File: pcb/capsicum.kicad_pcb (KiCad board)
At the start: 2 copper layers, 68.6 x 88.9 mm, 70 parts, among them J2 Screw terminal, J3 USB-C 16+8 USB 2.0, Q1 NS2101P, Q2 BC817, SW1 SW_SPDT, SW3 SW_SPDT, U1 ESP32-C3-WROOM-02, U2 TQ33E-1, U3 AP2112K, U4 MCP73831

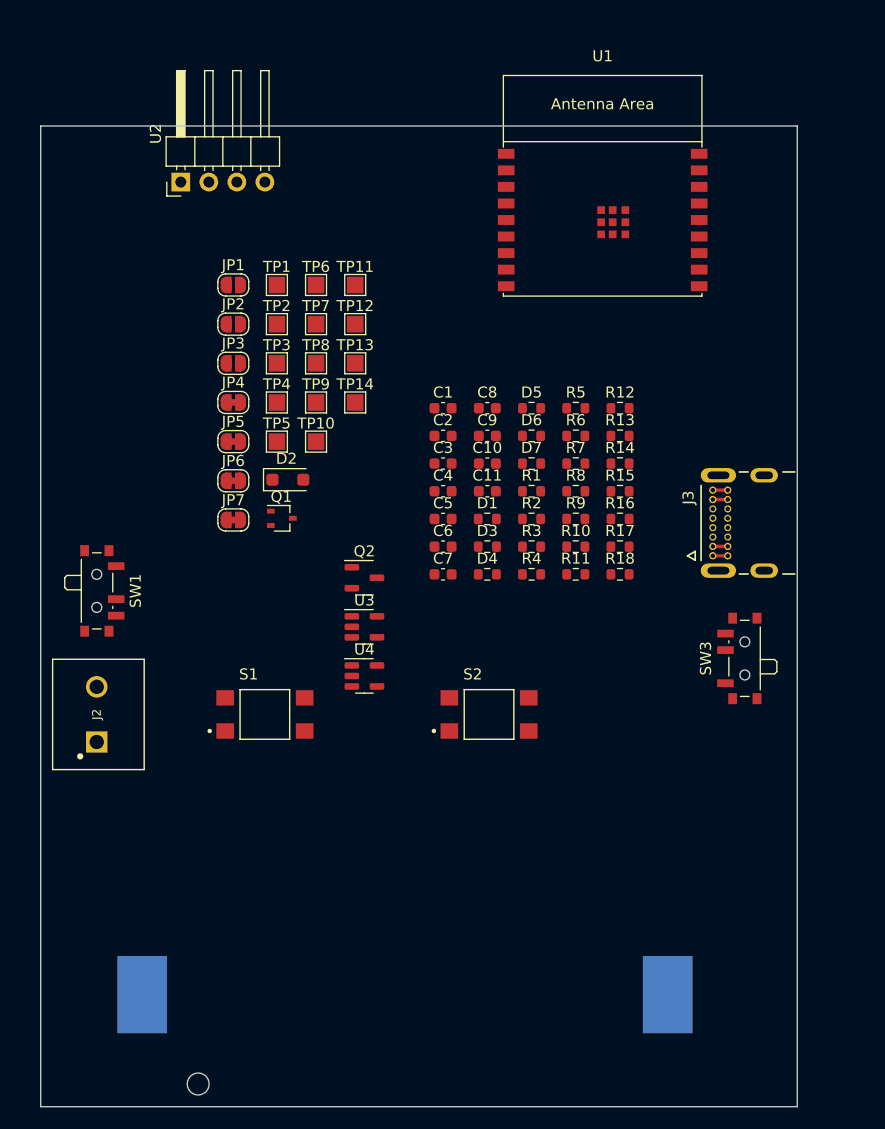
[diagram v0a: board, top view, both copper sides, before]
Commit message: feat: reorient all text to face upright on silkscreen layer
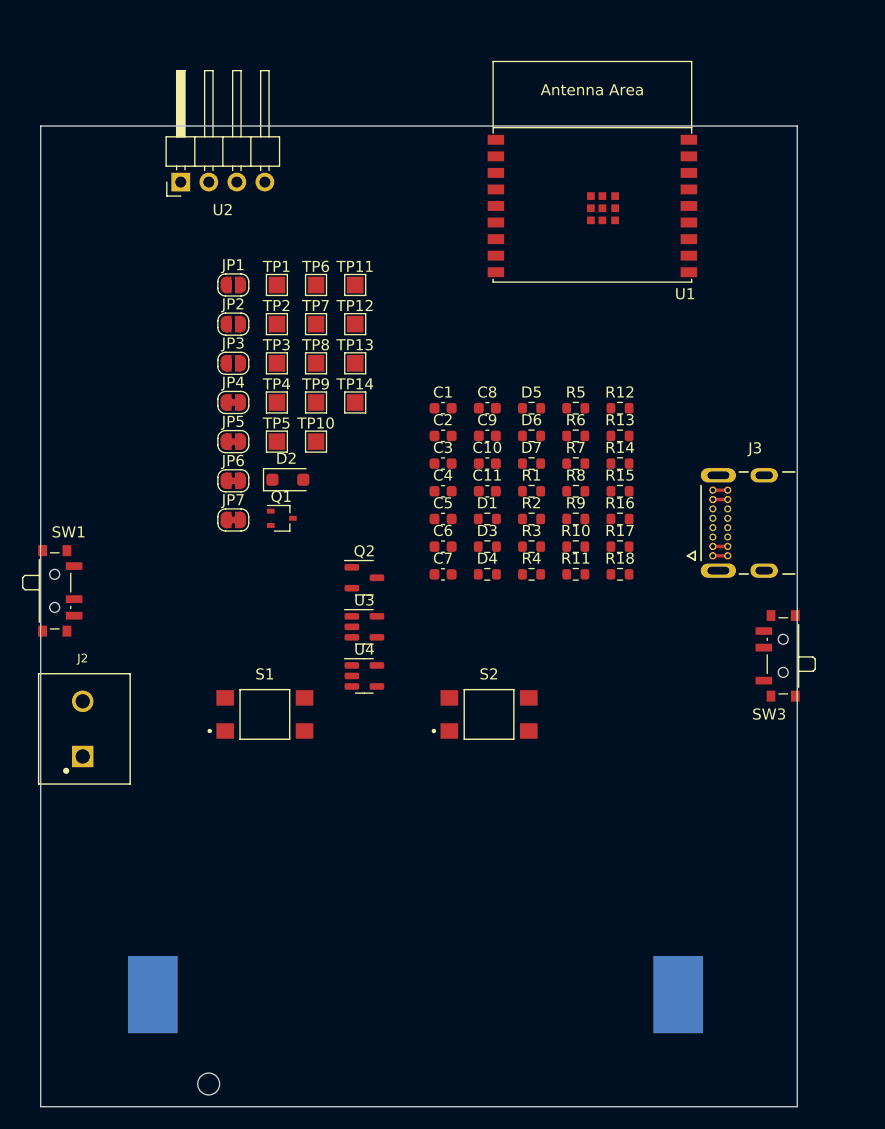
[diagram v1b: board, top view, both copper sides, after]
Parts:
- moved SW1 3.81 mm to (105.7, 92.9)
- moved SW3 3.49 mm to (171.1, 98.8)
- moved J2 1.82 mm to (108.0, 105.5)
- moved U1 1.57 mm to (154.2, 58.0)
- moved BT1 0.95 mm to (119.4, 129.5)

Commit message: feat: group components in the logic block USB-C, battery and charger
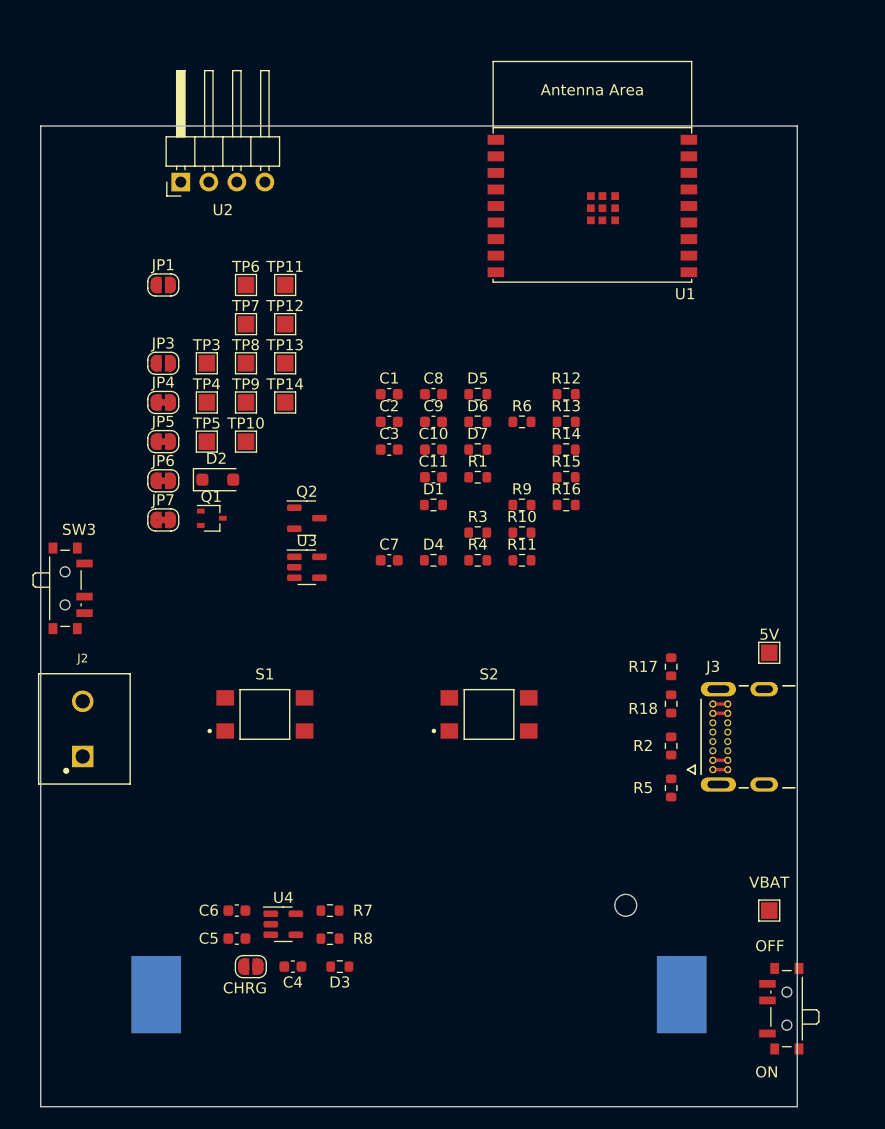
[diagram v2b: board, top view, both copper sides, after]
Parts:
- moved SW1 75.8 mm to (171.4, 130.8), turned to 90 degrees
- moved VBAT 69.4 mm to (170.2, 121.9)
- moved SW3 64.7 mm to (106.7, 92.7), turned to -90 degrees
- moved JP2 58.3 mm to (123.2, 127.0)
- moved 5V 55.7 mm to (170.2, 98.5)
- moved R8 46.3 mm to (130.4, 124.5)
- moved R7 46.2 mm to (130.4, 121.9), turned to 180 degrees
- moved C4 45.2 mm to (127.0, 127.0), turned to 180 degrees
- moved C5 42.4 mm to (121.9, 124.5), turned to 180 degrees
- moved D3 40.3 mm to (131.3, 127.0), turned to 180 degrees
- moved C6 37.9 mm to (121.9, 121.9), turned to 180 degrees
- moved BT1 37.8 mm to (157.2, 129.5), turned to 90 degrees
- moved R5 35.5 mm to (161.3, 110.8), turned to 90 degrees
- moved R2 24.2 mm to (161.3, 107.0), turned to -90 degrees
- moved U4 23.7 mm to (126.1, 123.2)
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- renumbered TP1 to 5V, TP2 to VBAT
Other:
- board text added: "CHRG"
- board text added: "OFF"
- board text added: "ON"

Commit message: feat: group components from batt measurement logical block in layout
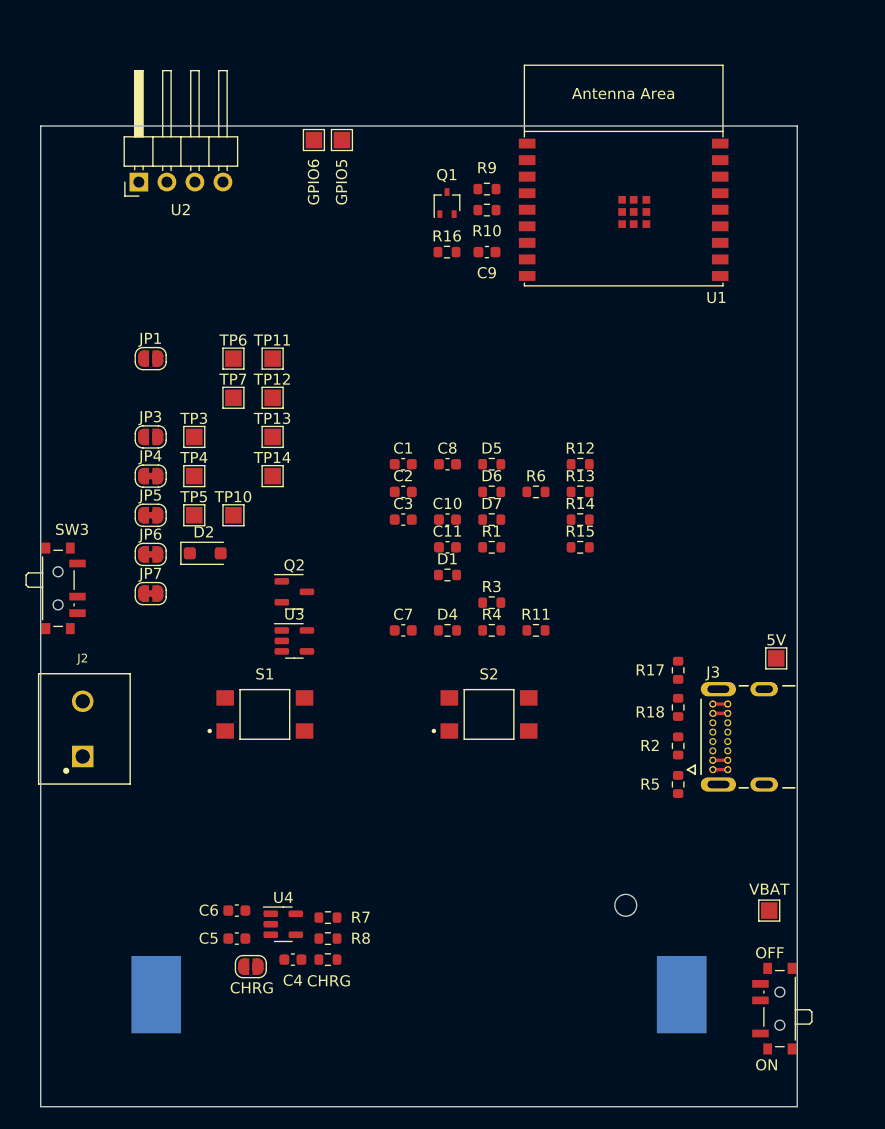
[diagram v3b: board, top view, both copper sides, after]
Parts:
- moved Q1 35.7 mm to (141.0, 57.8), turned to 90 degrees
- moved R10 29.4 mm to (144.6, 58.4)
- moved R9 28.8 mm to (144.6, 56.5), turned to 180 degrees
- moved R16 25.3 mm to (141.0, 62.2)
- moved TP9 25.3 mm to (131.4, 52.1)
- moved TP8 21.2 mm to (128.9, 52.1)
- moved C9 16.1 mm to (144.6, 62.2)
- moved Q2 6.77 mm to (127.1, 93.0)
- moved JP1 6.77 mm to (114.1, 71.9)
- moved JP6 6.77 mm to (114.1, 89.6)
- moved TP11 6.77 mm to (125.2, 71.9)
- moved TP6 6.77 mm to (121.6, 71.9)
- moved U3 6.77 mm to (127.1, 97.5)
- moved JP3 6.77 mm to (114.1, 79.0)
- moved JP4 6.77 mm to (114.1, 82.5)
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
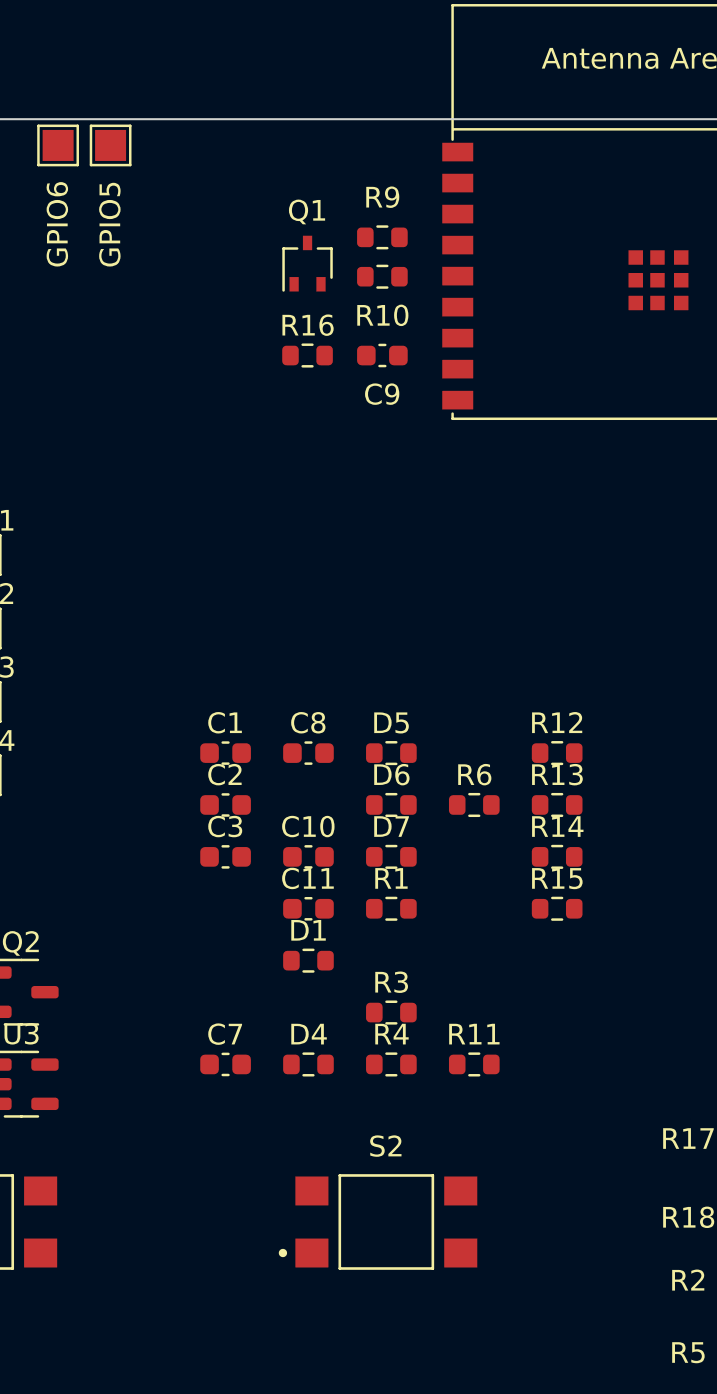
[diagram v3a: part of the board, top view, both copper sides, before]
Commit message: feat: group components from reset mcu logical block in layout
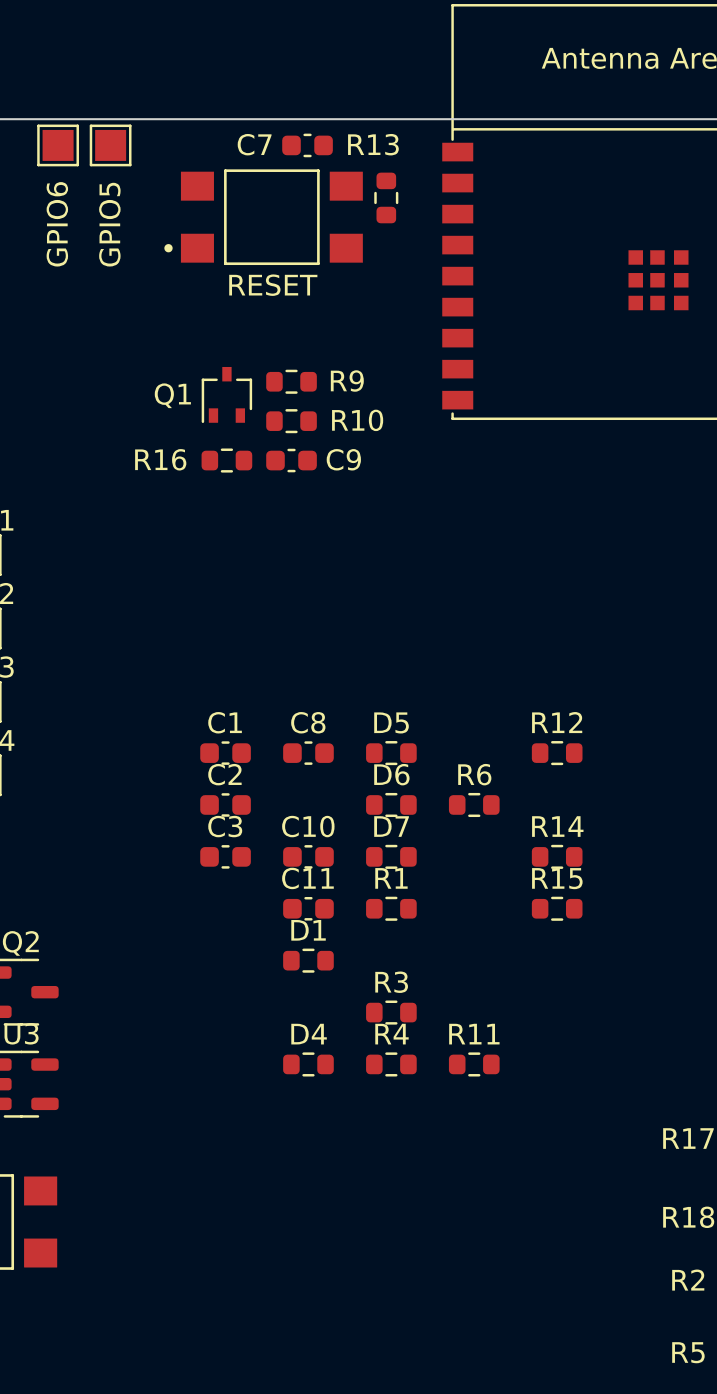
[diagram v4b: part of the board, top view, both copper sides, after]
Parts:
- moved S2 48.9 mm to (139.2, 55.5)
- moved C7 44.6 mm to (141.0, 52.1), turned to 180 degrees
- moved R13 30.5 mm to (144.8, 54.6), turned to 90 degrees
- moved R10 8.25 mm to (140.2, 65.4)
- moved R9 8.25 mm to (140.2, 63.5)
- moved Q1 7.45 mm to (137.1, 64.1)
- moved C9 6.72 mm to (140.2, 67.3)
- moved R16 6.40 mm to (137.1, 67.3)
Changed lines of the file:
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@@
   )
   (footprint "Resistor_SMD:R_0603_1608Metric" (layer "F.Cu")
-    (at 144.59 58.42)
+    (at 140.195 65.405)
     (descr "Resistor SMD 0603 (1608 Metric), square (rectangular) end terminal, IPC_7351 nominal, (Body size source: IPC-SM-782 page 72, https://www.pcb-3d.com/wordpress/wp-content/uploads/ipc-sm-782a_amendment_1_and_2.pdf), generated with kicad-footprint-generator")
     (tags "resistor")
@@
     (property "ki_keywords" "R resistor")
     (attr smd)
-    (fp_text reference "R10" (at 0 1.905) (layer "F.SilkS")
+    (fp_text reference "R10" (at 3.175 0) (layer "F.SilkS")
         (effects (font (size 1 1) (thickness 0.15)))
     )
@@
   )
   (footprint "Push button:SW_TL3305AF160QG" (layer "F.Cu")
-    (at 144.78 104.14)
+    (at 139.245 55.54)
     (property "Category" "Connector")
     (property "DNP" "")
@@
     (property "Unit Price (USD)" "0.1701")
     (attr smd)
-    (fp_text reference "S2" (at 0 -3.635) (layer "F.SilkS")
+    (fp_text reference "S2" (at 0 3.325) (layer "F.SilkS") hide
         (effects (font (size 1 1) (thickness 0.15)))
     )
@@
         (effects (font (size 1 1) (thickness 0.15)))
     )
+    (fp_text user "RESET" (at 0 3.325 unlocked) (layer "F.SilkS")
+        (effects (font (size 1 1) (thickness 0.15)))
+    )
     (fp_line (start -2.25 -2.25) (end 2.25 -2.25)
       (stroke (width 0.127) (type solid)) (layer "F.SilkS"))
@@
   )
   (footprint "Capacitor_SMD:C_0603_1608Metric" (layer "F.Cu")
-    (at 144.59 62.23)
+    (at 140.195 67.31)
     (descr "Capacitor SMD 0603 (1608 Metric), square (rectangular) end terminal, IPC_7351 nominal, (Body size source: IPC-SM-782 page 76, https://www.pcb-3d.com/wordpress/wp-content/uploads/ipc-sm-782a_amendment_1_and_2.pdf), generated with kicad-footprint-generator")
     (tags "capacitor")
@@
     (property "ki_keywords" "capacitor cap")
     (attr smd)
-    (fp_text reference "C9" (at 0 1.905) (layer "F.SilkS")
+    (fp_text reference "C9" (at 2.54 0) (layer "F.SilkS")
         (effects (font (size 1 1) (thickness 0.15)))
     )
@@
   )
   (footprint "Capacitor_SMD:C_0603_1608Metric" (layer "F.Cu")
-    (at 137.005 96.52)
+    (at 140.97 52.07 180)
     (descr "Capacitor SMD 0603 (1608 Metric), square (rectangular) end terminal, IPC_7351 nominal, (Body size source: IPC-SM-782 page 76, https://www.pcb-3d.com/wordpress/wp-content/uploads/ipc-sm-782a_amendment_1_and_2.pdf), generated with kicad-footprint-generator")
     (tags "capacitor")
@@
     (property "ki_keywords" "capacitor cap")
     (attr smd)
-    (fp_text reference "C7" (at 0 -1.43) (layer "F.SilkS")
+    (fp_text reference "C7" (at 2.54 0) (layer "F.SilkS")
         (effects (font (size 1 1) (thickness 0.15)))
     )
@@
     (fp_line (start 0.8 0.4) (end -0.8 0.4)
       (stroke (width 0.1) (type solid)) (layer "F.Fab"))
-    (pad "1" smd roundrect (at -0.775 0) (size 0.9 0.95) (layers "F.Cu" "F.Paste" "F.Mask") (roundrect_rratio 0.25)
+    (pad "1" smd roundrect (at -0.775 0 180) (size 0.9 0.95) (layers "F.Cu" "F.Paste" "F.Mask") (roundrect_rratio 0.25)
       (net 6 "/RESET") (pintype "passive"))
-    (pad "2" smd roundrect (at 0.775 0) (size 0.9 0.95) (layers "F.Cu" "F.Paste" "F.Mask") (roundrect_rratio 0.25)
+    (pad "2" smd roundrect (at 0.775 0 180) (size 0.9 0.95) (layers "F.Cu" "F.Paste" "F.Mask") (roundrect_rratio 0.25)
       (net 2 "GND") (pintype "passive"))
     (model "${KICAD6_3DMODEL_DIR}/Capacitor_SMD.3dshapes/C_0603_1608Metric.wrl"
@@
   )
   (footprint "Resistor_SMD:R_0603_1608Metric" (layer "F.Cu")
-    (at 153.045 83.97)
+    (at 144.78 54.61 90)
     (descr "Resistor SMD 0603 (1608 Metric), square (rectangular) end terminal, IPC_7351 nominal, (Body size source: IPC-SM-782 page 72, https://www.pcb-3d.com/wordpress/wp-content/uploads/ipc-sm-782a_amendment_1_and_2.pdf), generated with kicad-footprint-generator")
     (tags "resistor")
@@
     (property "ki_keywords" "R resistor")
     (attr smd)
-    (fp_text reference "R13" (at 0 -1.43) (layer "F.SilkS")
+    (fp_text reference "R13" (at 2.54 -0.635 180) (layer "F.SilkS")
         (effects (font (size 1 1) (thickness 0.15)))
     )
-    (fp_text value "10k" (at 0 1.43) (layer "F.Fab")
+    (fp_text value "10k" (at 0 1.43 90) (layer "F.Fab")
         (effects (font (size 1 1) (thickness 0.15)))
     )
-    (fp_text user "${REFERENCE}" (at 0 0) (layer "F.Fab")
+    (fp_text user "${REFERENCE}" (at 0 0 90) (layer "F.Fab")
         (effects (font (size 0.4 0.4) (thickness 0.06)))
     )
@@
     (fp_line (start 0.8 0.4125) (end -0.8 0.4125)
       (stroke (width 0.1) (type solid)) (layer "F.Fab"))
-    (pad "1" smd roundrect (at -0.825 0) (size 0.8 0.95) (layers "F.Cu" "F.Paste" "F.Mask") (roundrect_rratio 0.25)
+    (pad "1" smd roundrect (at -0.825 0 90) (size 0.8 0.95) (layers "F.Cu" "F.Paste" "F.Mask") (roundrect_rratio 0.25)
       (net 10 "+3V3") (pintype "passive"))
-    (pad "2" smd roundrect (at 0.825 0) (size 0.8 0.95) (layers "F.Cu" "F.Paste" "F.Mask") (roundrect_rratio 0.25)
+    (pad "2" smd roundrect (at 0.825 0 90) (size 0.8 0.95) (layers "F.Cu" "F.Paste" "F.Mask") (roundrect_rratio 0.25)
       (net 6 "/RESET") (pintype "passive"))
     (model "${KICAD6_3DMODEL_DIR}/Resistor_SMD.3dshapes/R_0603_1608Metric.wrl"
@@
   )
   (footprint "Package_TO_SOT_SMD:SOT-323_SC-70" (layer "F.Cu")
-    (at 140.97 57.785 90)
+    (at 137.07 64.135 90)
     (descr "SOT-323, SC-70")
     (tags "SOT-323 SC-70")
@@
     (property "ki_keywords" "P-Channel MOSFET")
     (attr smd)
-    (fp_text reference "Q1" (at 2.54 0 180) (layer "F.SilkS")
+    (fp_text reference "Q1" (at 0 -2.59 180) (layer "F.SilkS")
         (effects (font (size 1 1) (thickness 0.15)))
     )
@@
   )
   (footprint "Resistor_SMD:R_0603_1608Metric" (layer "F.Cu")
-    (at 144.59 56.515 180)
+    (at 140.195 63.5 180)
     (descr "Resistor SMD 0603 (1608 Metric), square (rectangular) end terminal, IPC_7351 nominal, (Body size source: IPC-SM-782 page 72, https://www.pcb-3d.com/wordpress/wp-content/uploads/ipc-sm-782a_amendment_1_and_2.pdf), generated with kicad-footprint-generator")
     (tags "resistor")
@@
     (property "ki_keywords" "R resistor")
     (attr smd)
-    (fp_text reference "R9" (at 0 1.905) (layer "F.SilkS")
+    (fp_text reference "R9" (at -2.68 0) (layer "F.SilkS")
         (effects (font (size 1 1) (thickness 0.15)))
     )
@@
   )
   (footprint "Resistor_SMD:R_0603_1608Metric" (layer "F.Cu")
-    (at 140.97 62.23)
+    (at 137.07 67.31)
     (descr "Resistor SMD 0603 (1608 Metric), square (rectangular) end terminal, IPC_7351 nominal, (Body size source: IPC-SM-782 page 72, https://www.pcb-3d.com/wordpress/wp-content/uploads/ipc-sm-782a_amendment_1_and_2.pdf), generated with kicad-footprint-generator")
     (tags "resistor")
@@
     (property "ki_keywords" "R resistor")
     (attr smd)
-    (fp_text reference "R16" (at 0 -1.43) (layer "F.SilkS")
+    (fp_text reference "R16" (at -3.225 0) (layer "F.SilkS")
         (effects (font (size 1 1) (thickness 0.15)))
     )
